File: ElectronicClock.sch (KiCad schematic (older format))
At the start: 93 parts, among them U4 74LS08

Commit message: Associated components with footprints
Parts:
- removed R? (x41): R, symbol R
- added R10, R17, R19, R20, R21, R23, R24, R25, R27, R28, R29, R30, R32, R33, R34, R35, R36, R37, R38, R39, R40, R41, R44, R45, R46, R47, R48, R49, R5, R50, R51, R52, R53, R54, R55, R56, R57, R6, R7, R8, R9: R, Resistors_THT:R_Axial_DIN0204_L3.6mm_D1.6mm_P7.62mm_Horizontal, symbol R
- C1, C2: renamed from C?; footprint (none) -> Capacitors_THT:C_Disc_D3.0mm_W2.0mm_P2.50mm
- D1, D2: renamed from D?; footprint (none) -> Diodes_THT:D_DO-41_SOD81_P7.62mm_Horizontal
- DP1, DP2, DP3, DP4, DP5, DP6: renamed from DP?; footprint (none) -> Displays_7-Segment:7SegmentLED_LTS6760_LTS6780
- IC1: renamed from IC?; footprint 40xx-DIL16 -> Housings_DIP:DIP-16_W7.62mm_Socket_LongPads
- R1, R11, R12, R13, R14, R15, R16, R18, R2, R22, R26, R3, R31, R4, R42, R43: renamed from R?; footprint (none) -> Resistors_THT:R_Axial_DIN0204_L3.6mm_D1.6mm_P7.62mm_Horizontal
- SW1, SW2, SW4, SW5, SW6, SW7: renamed from SW?; footprint (none) -> Buttons_Switches_THT:SW_PUSH_6mm
- U1, U11, U12, U14, U3, U5, U7, U8: renamed from U?; footprint (none) -> Housings_DIP:DIP-14_W7.62mm_Socket_LongPads
- U10, U13, U15, U2, U6, U9: renamed from U?; footprint (none) -> Housings_DIP:DIP-16_W7.62mm_Socket_LongPads
- U4: footprint (none) -> Housings_DIP:DIP-14_W7.62mm_Socket_LongPads
- Y1: renamed from Y?; footprint (none) -> Crystals:Crystal_DS10_d1.0mm_l4.3mm_Horizontal_1EP_style1
- gave numbers to parts that had none: 1
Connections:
- net 1/10Hz: now also R13.2, SW2.2
- net 1/36000Hz: now also R22.2, SW7.2
- net 1/3600Hz: now also R18.2, SW6.2
- net 1/600Hz: now also R15.2, SW5.2
- net 1/60Hz: now also R14.2, SW4.2
- net 1Hz: now also R12.2, SW1.2
- net GND: now also SW3.4 (A), U1.10 (GND), U12.10 (GND), U14.10 (GND), U5.10 (GND), U7.10 (GND), U8.10 (GND)
- net at U2.10 (d): now also R8.1
- net at U2.11 (c): now also R9.1
- net at U2.12 (b): now also R10.1
- net at U2.14 (g): now also R5.1
- net at U2.15 (f): now also R6.1
- net at U2.9 (e): now also R7.1
- net at U6.10 (d): now also R21.1
- net at U6.11 (c): now also R23.1
- net at U6.12 (b): now also R24.1
- net at U6.13 (a): now also R25.1
- net at U6.14 (g): now also R17.1
- net at U6.15 (f): now also R19.1
- net at U6.9 (e): now also R20.1
- net at DP1.1 (e): now also R7.2
- net at DP1.10 (g): now also R5.2
- net at DP1.2 (d): now also R8.2
- net at DP1.4 (c): now also R9.2
- net at DP1.6 (b): now also R10.2
- net at DP1.9 (f): now also R6.2
- net at DP2.1 (e): now also R20.2
- net at DP2.10 (g): now also R17.2
- net at DP2.2 (d): now also R21.2
- net at DP2.4 (c): now also R23.2
- net at DP2.6 (b): now also R24.2
- net at DP2.7 (a): now also R25.2
- net at DP2.9 (f): now also R19.2
- net at U10.10 (d): now also R38.1
- net at U10.11 (c): now also R39.1
- net at U10.12 (b): now also R40.1
- net at U10.13 (a): now also R41.1
- net at U10.14 (g): now also R32.1
- net at U10.15 (f): now also R34.1
- net at U10.9 (e): now also R36.1
- net at U13.10 (d): now also R48.1
- net at U13.11 (c): now also R47.1
- net at U13.12 (b): now also R46.1
- net at U13.13 (a): now also R45.1
- net at U13.14 (g): now also R51.1
- net at U13.15 (f): now also R50.1
- net at U13.9 (e): now also R49.1
- net at DP4.1 (e): now also R36.2
- net at DP4.10 (g): now also R32.2
- net at DP4.2 (d): now also R38.2
- net at DP4.4 (c): now also R39.2
- net at DP4.6 (b): now also R40.2
- net at DP4.7 (a): now also R41.2
- net at DP4.9 (f): now also R34.2
- net at DP6.1 (e): now also R49.2
- net at DP6.10 (g): now also R51.2
- net at DP6.2 (d): now also R48.2
- net at DP6.4 (c): now also R47.2
- net at DP6.6 (b): now also R46.2
- net at DP6.7 (a): now also R45.2
- net at DP6.9 (f): now also R50.2
- net at U9.10 (d): now also R30.1
- net at U9.11 (c): now also R33.1
- net at U9.12 (b): now also R35.1
- net at U9.13 (a): now also R37.1
- net at U9.14 (g): now also R27.1
- net at U9.15 (f): now also R28.1
- net at U9.9 (e): now also R29.1
- net at U15.10 (d): now also R54.1
- net at U15.11 (c): now also R55.1
- net at U15.12 (b): now also R56.1
- net at U15.13 (a): now also R57.1
- net at U15.14 (g): now also R44.1
- net at U15.15 (f): now also R52.1
- net at U15.9 (e): now also R53.1
- net at DP3.1 (e): now also R29.2
- net at DP3.10 (g): now also R27.2
- net at DP3.2 (d): now also R30.2
- net at DP3.4 (c): now also R33.2
- net at DP3.6 (b): now also R35.2
- net at DP3.7 (a): now also R37.2
- net at DP3.9 (f): now also R28.2
- net at DP5.1 (e): now also R53.2
- net at DP5.10 (g): now also R44.2
- net at DP5.2 (d): now also R54.2
- net at DP5.4 (c): now also R55.2
- net at DP5.6 (b): now also R56.2
- net at DP5.7 (a): now also R57.2
- net at DP5.9 (f): now also R52.2
- no-connect marks 30 -> 27
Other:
- moved on the sheet: R12, R13, R14, R15, R18, R22, SW1, SW2, SW3A, SW3B, SW4, SW5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

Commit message: Finished up the schematic, generated netlist, exported to PDF
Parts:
- C1: value C -> 10p
- C2: value C -> 22p
- R1: value R -> 470k
- R10, R11, R16, R17, R19, R20, R21, R23, R24, R25, R26, R27, R28, R29, R30, R31, R32, R33, R34, R35, R36, R37, R38, R39, R4, R40, R41, R42, R43, R44, R45, R46, R47, R48, R49, R5, R50, R51, R52, R53, R54, R55, R56, R57, R6, R7, R8, R9: value R -> 1k
- R12, R13, R14, R15, R18, R22: value R -> 10k
- R2: value R -> 10M
- SW3: footprint (none) -> switch_dpdt:SWITCH_DPDT_8x8mm
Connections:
- net GND: no longer U1.10 (GND), U12.10 (GND), U14.10 (GND), U5.10 (GND), U7.10 (GND), U8.10 (GND)

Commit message: Reworked the component names
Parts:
- renumbered C1 to C0, C2 to C1, U7 to CTR_H0, U12 to CTR_H1, U8 to CTR_M0, U14 to CTR_M1, U1 to CTR_S0, U5 to CTR_S1, DP3 to DP_H0, DP5 to DP_H1, DP4 to DP_M0, DP6 to DP_M1, DP1 to DP_S0, DP2 to DP_S1, U9 to DRV_H0, U15 to DRV_H1, U10 to DRV_M0, U13 to DRV_M1, U2 to DRV_S0, U6 to DRV_S1, R2 to R0, R16 to R10, R31 to R11, R42 to R12, R26 to R13, R43 to R14, R5 to R15, R6 to R16, R7 to R17, R8 to R18, R9 to R19, R3 to R2, R10 to R20, R11 to R21, R17 to R22, R19 to R23, R20 to R24, R21 to R25, R23 to R26, R24 to R27, R25 to R28, R32 to R29, R12 to R3, R34 to R30, R36 to R31, R38 to R32, R39 to R33, R40 to R34, R41 to R35, R51 to R36, R50 to R37, R49 to R38, R48 to R39, R13 to R4, R47 to R40, R46 to R41, R45 to R42, R27 to R43, R28 to R44, R29 to R45, R30 to R46, R33 to R47, R35 to R48, R37 to R49, R14 to R5, R44 to R50, R52 to R51, R53 to R52, R54 to R53, R55 to R54, R56 to R55, R57 to R56, R15 to R6, R18 to R7, R22 to R8, R4 to R9, SW3 to SW0, SW4 to SW3, SW5 to SW4, SW6 to SW5, SW7 to SW6, IC1 to U0, U3 to U1, U4 to U2, U11 to U3, Y1 to X1

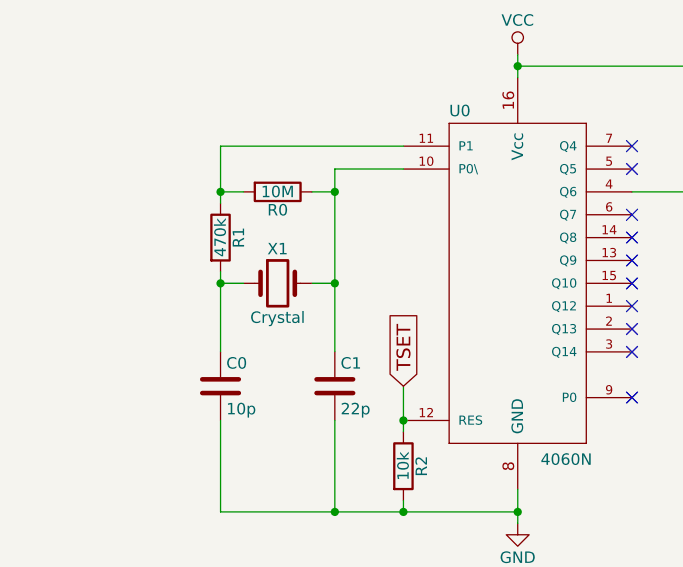
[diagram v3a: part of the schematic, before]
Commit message: Routed 3 displays
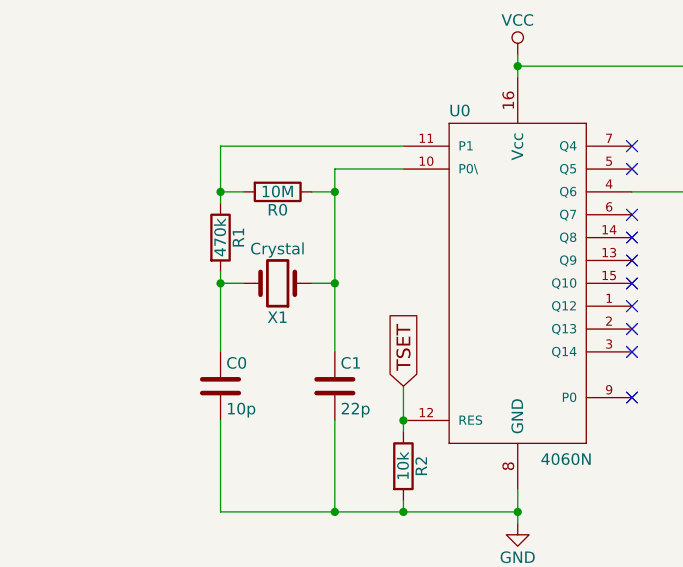
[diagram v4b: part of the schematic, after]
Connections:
- net at C0.1, R1.2: now also X1.2; no longer X1.1
- net at C1.1, R0.1, U0.10 (P0\): now also X1.1; no longer X1.2
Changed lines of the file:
@@
 F 3 "" H 1750 2350 50  0000 C CNN
 	1    1750 2350
-	1    0    0    -1
+	-1   0    0    1
 $EndComp
 $Comp
